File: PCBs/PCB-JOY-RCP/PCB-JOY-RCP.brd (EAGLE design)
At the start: 30 x 25.9 mm, 20 parts, among them IC1 ADS7828

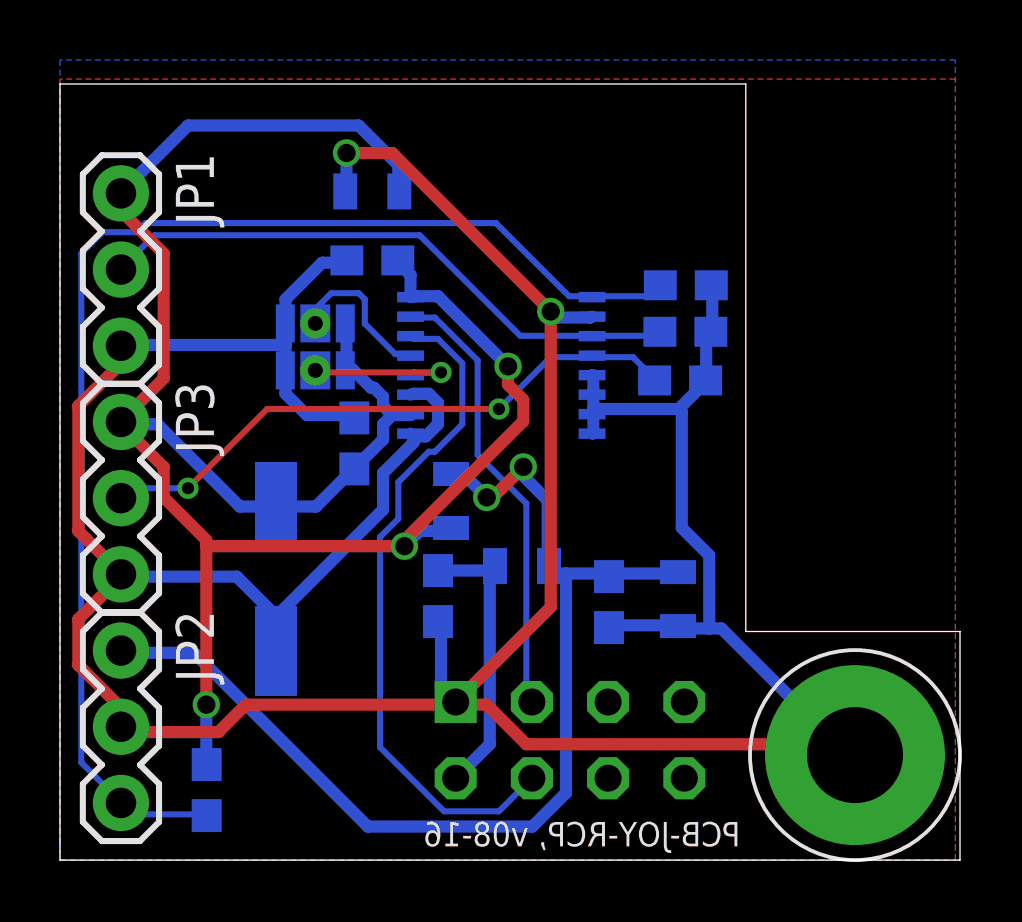
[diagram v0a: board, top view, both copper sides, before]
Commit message: Added SKAARHOJ_ID to a lot of PCBs...
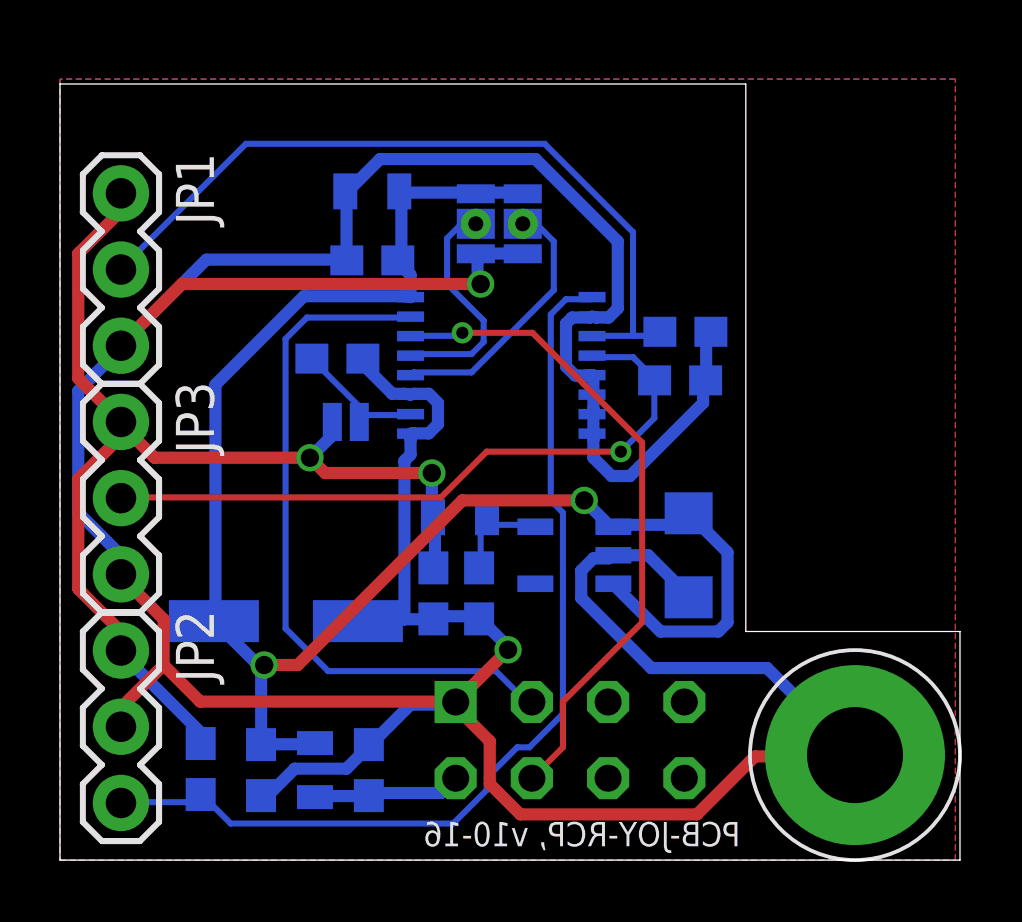
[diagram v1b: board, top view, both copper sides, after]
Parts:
- removed C9: 22uF, SparkFun:0805
- removed PC2: 47u, rcl:PANASONIC_D
- added C23: 10uF 6.3V A TANT, freetronics:EIA3216
- added C5: 100nF, SparkFun:0603-CAP
- added PC1: 330uF, rcl:PANASONIC_D
- added SJ1: SOLDERJUMPERNO, SparkFun:SJ_2S-NO
- added U2: MIC5205-3.3YM5, microbuilder:SOT23-5
- C4: value 10n -> 100nF
- moved C10 12.9 mm to (6.70, 3.00)
- moved C4 12.4 mm to (14.0, 8.89), turned to 270 degrees
- moved L4 9.69 mm to (8.50, 3.00), turned to 90 degrees
- moved U$19 6.30 mm to (13.9, 21.2), turned to 0 degrees
- moved C12 6.24 mm to (10.3, 3.00), turned to 90 degrees
- moved C1 2.88 mm to (9.24, 16.7), turned to 180 degrees
- moved R2 0.73 mm to (4.69, 3.04)
- moved L1 0.62 mm to (13.3, 11.4), turned to 0 degrees
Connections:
- removed net 5V_AD: C1.1, C2.1, C3.1, IC1.10, IC1.16, JP1.1, JP3.1, L1.1, PC2.+, R2.1, U$19.H0, U$19.H1
- new net N$1: C1.1, IC1.10, SJ1.2
- new net N$3: C4.1, L1.1, U2.5
- new net REF: C5.1, JP1.1, JP2.1, JP3.1, L1.2, R2.1, SJ1.1
- net 5V: now also C2.1, C23.A, C3.1, IC1.16, PC1.+, U$19.H0, U$19.H1, U2.1, U2.3; no longer C9.1, JP2.1, L1.2
- net FRONT: no longer C4.1
- net GND: now also C23.C, C5.2, PC1.-, U2.2; no longer C9.2, PC2.-
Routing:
- net 5V_AD: track 71.5 -> 0.00 mm, vias 3 -> 0
- net REF: track 0.00 -> 37.7 mm, vias 0 -> 2
- net 5V: track 36.4 -> 56.0 mm
- net FRONT: track 42.8 -> 32.1 mm
- net GND: track 129.9 -> 139.7 mm
- net I2C_SDA: track 15.0 -> 23.4 mm
- net JOY_1: track 19.9 -> 25.8 mm
- net N$1: track 0.00 -> 4.85 mm
- net ARD_5V: track 9.55 -> 4.93 mm
- net A0: track 5.33 -> 8.91 mm, vias 1 -> 0
- net N$3: track 0.00 -> 3.54 mm
- net A1: track 5.26 -> 7.81 mm
- net JOY_2: track 20.1 -> 22.6 mm, vias 2 -> 1
- net I2C_SCL: track 22.6 -> 22.0 mm, vias 0 -> 1
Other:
- board text added: "PCB-JOY-RCP, v10-16"
- board text removed: "PCB-JOY-RCP, v08-16"

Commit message: PCB updates
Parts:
- added U$1: GNDPAD6MM, SKAARHOJ:3.2MMPAD6MM
- moved U$6 53.7 mm to (3.50, 52.0), turned to 180 degrees
- moved SERIAL 45.1 mm to (13.0, 49.0), turned to 90 degrees
- moved C10 41.2 mm to (13.8, 43.6), turned to 90 degrees
- moved L4 40.8 mm to (12.0, 43.6), turned to 270 degrees
- moved C12 40.6 mm to (10.2, 43.6), turned to 270 degrees
- moved R2 30.5 mm to (16.3, 31.2), turned to 180 degrees
- moved PC1 30.3 mm to (11.7, 38.0), turned to 180 degrees
- moved C23 24.5 mm to (10.4, 32.2), turned to 0 degrees
- moved JP2 22.2 mm to (16.5, 23.8), turned to 90 degrees
- moved JP1 20.0 mm to (16.5, 8.51), turned to 90 degrees
- moved U2 19.5 mm to (10.4, 28.4), turned to 180 degrees
- moved U$19 18.8 mm to (16.1, 2.54), turned to 180 degrees
- moved C4 16.5 mm to (11.7, 25.2), turned to 180 degrees
- moved C6 15.1 mm to (9.15, 8.04), turned to 0 degrees
- moved C5 14.8 mm to (11.7, 23.7), turned to 180 degrees
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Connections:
- net GND: now also U$1.P$1
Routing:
- net I2C_SCL: track 22.0 -> 42.8 mm
- net I2C_SDA: track 23.4 -> 39.4 mm, vias 0 -> 1
- net GND: track 139.7 -> 124.1 mm, vias 2 -> 3
- net A0: track 8.91 -> 17.9 mm, vias 0 -> 1
- net 5V: track 56.0 -> 64.7 mm, vias 2 -> 3
- net A1: track 7.81 -> 15.3 mm, vias 0 -> 1
- net JOY_2: track 22.6 -> 17.1 mm, vias 1 -> 2
- net ARD_5V: track 4.93 -> 9.89 mm
- net JOY_1: track 25.8 -> 30.7 mm, vias 0 -> 1
- net FRONT: track 32.1 -> 29.0 mm, vias 0 -> 2
- net REF: track 37.7 -> 40.5 mm, vias 2 -> 1
- net N$1: track 4.85 -> 7.46 mm
- removed copper zone on layer 1, net GND
- removed copper zone on layer 16, net GND
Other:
- board size 30 x 25.9 mm -> 18 x 55.5 mm
- board text added: "PCB-JOY-RCP, v10-16b"
- board text removed: "PCB-JOY-RCP, v10-16"

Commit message: Added cap for silencing the regulator
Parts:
- added C8: 10uF 6.3V A TANT, freetronics:EIA3216
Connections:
- net GND: now also C8.C
- net REF: now also C8.A
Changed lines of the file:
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@@
 </element>
 <element name="U$1" library="SKAARHOJ" package="3.2MMPAD6MM" value="GNDPAD6MM" x="3.5" y="3.5" rot="R180"/>
+<element name="C8" library="freetronics" package="EIA3216" value="10uF 6.3V A TANT" x="-22.86" y="-29.21"/>
 </elements>
 <signals>
@@
 <via x="9.2456" y="12.9032" extent="1-16" drill="0.6096"/>
 <via x="9.2456" y="15.748" extent="1-16" drill="0.6096"/>
+<contactref element="C8" pad="C"/>
+<wire x1="3.5" y1="3.5" x2="-24.26" y2="-29.21" width="0" layer="19" extent="1-1"/>
 </signal>
 <signal name="A1">
@@
 <wire x1="13.4112" y1="22.7584" x2="13.3096" y2="22.86" width="0.3048" layer="16"/>
 <via x="15.3416" y="6.1976" extent="1-16" drill="0.6096"/>
+<contactref element="C8" pad="A"/>
+<wire x1="15.3416" y1="6.1976" x2="-21.46" y2="-29.21" width="0" layer="19" extent="1-16"/>
 </signal>
 <signal name="N$3">

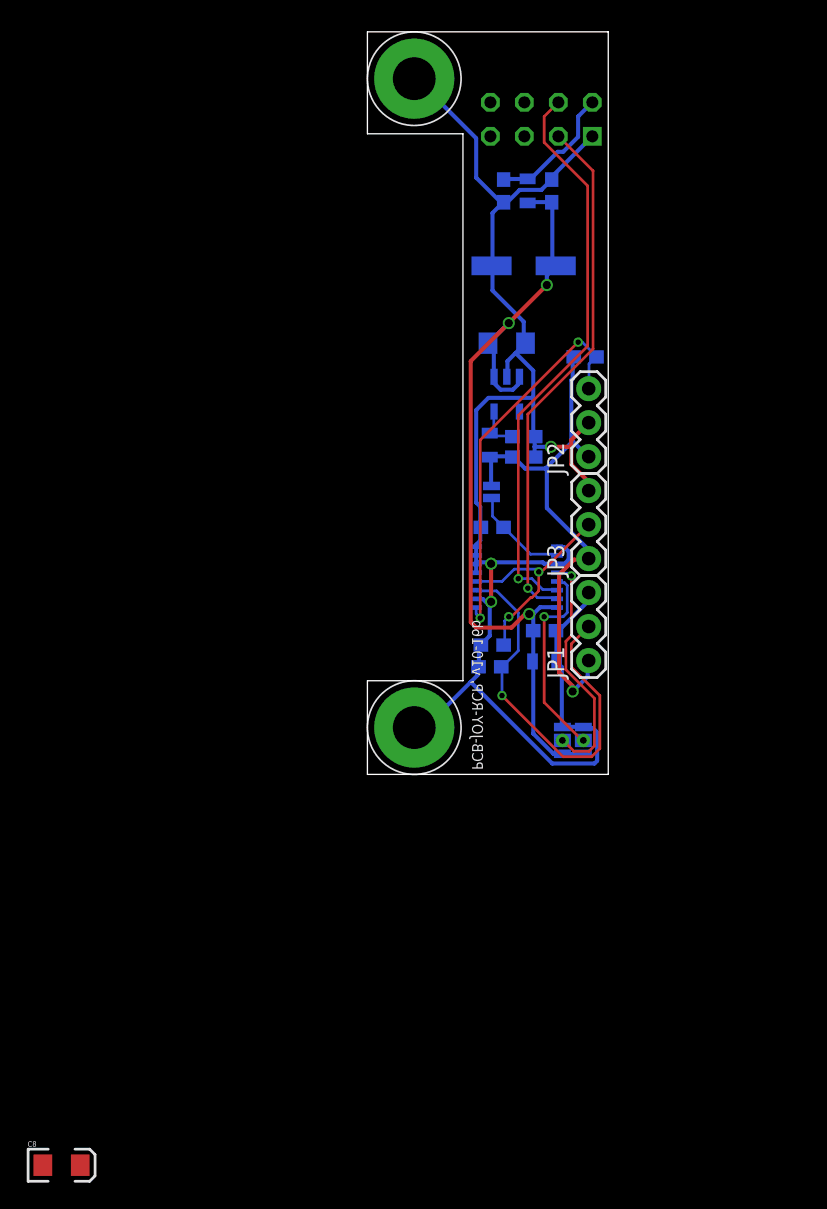
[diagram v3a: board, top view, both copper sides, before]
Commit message: Modified circuitry around AD converter on a number of PCBs
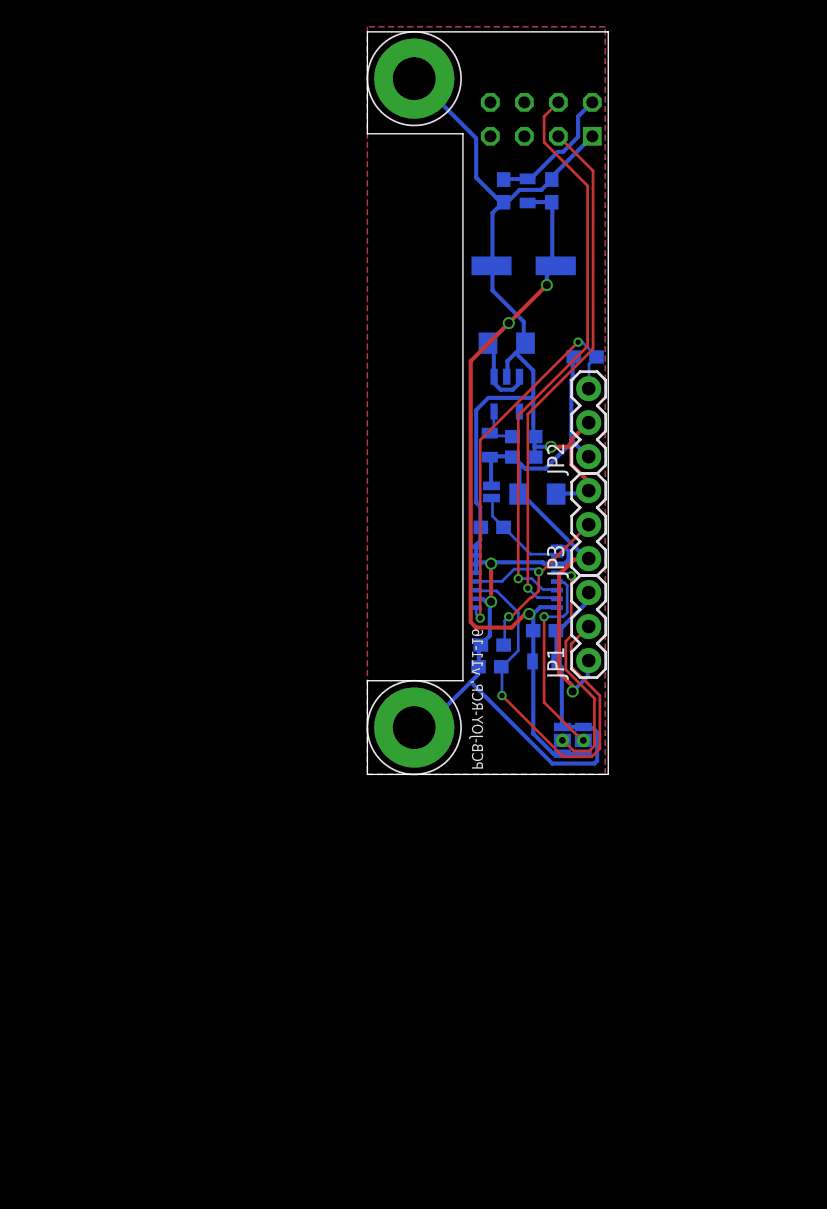
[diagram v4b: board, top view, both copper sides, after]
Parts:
- moved C8 61.5 mm to (12.7, 21.0), flipped to the bottom
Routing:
- net GND: track 124.1 -> 126.7 mm
- net REF: track 40.5 -> 42.8 mm
- added copper zone on layer 1, net GND
- added copper zone on layer 16, net GND
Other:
- board text added: "PCB-JOY-RCP, v11-16"
- board text removed: "PCB-JOY-RCP, v10-16b"
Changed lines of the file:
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@@
 <plain>
 <wire x1="18" y1="55.5" x2="0" y2="55.5" width="0" layer="20"/>
-<text x="7.823" y="0.335" size="0.8128" layer="121" ratio="12" rot="MR90">PCB-JOY-RCP, v10-16b</text>
+<text x="7.823" y="0.335" size="0.8128" layer="121" ratio="12" rot="MR90">PCB-JOY-RCP, v11-16</text>
 <wire x1="0" y1="0" x2="18" y2="0" width="0" layer="20"/>
 <wire x1="18" y1="55.5" x2="18" y2="0" width="0" layer="20"/>
@@
 </element>
 <element name="U$1" library="SKAARHOJ" package="3.2MMPAD6MM" value="GNDPAD6MM" x="3.5" y="3.5" rot="R180"/>
-<element name="C8" library="freetronics" package="EIA3216" value="10uF 6.3V A TANT" x="-22.86" y="-29.21"/>
+<element name="C8" library="freetronics" package="EIA3216" value="10uF 6.3V A TANT" x="12.7" y="20.955" rot="MR0"/>
 </elements>
 <signals>
@@
 <via x="9.2456" y="15.748" extent="1-16" drill="0.6096"/>
 <contactref element="C8" pad="C"/>
-<wire x1="3.5" y1="3.5" x2="-24.26" y2="-29.21" width="0" layer="19" extent="1-1"/>
+<wire x1="16.375" y1="21" x2="14.125" y2="21" width="0.3048" layer="16"/>
+<wire x1="16.5" y1="21.125" x2="16.375" y2="21" width="0.3048" layer="16"/>
+<wire x1="14.125" y1="21" x2="14.1" y2="20.955" width="0.3048" layer="16"/>
+<wire x1="16.5" y1="21.125" x2="16.538" y2="21.21" width="0.3048" layer="16"/>
+<polygon width="0.254" layer="1">
+<vertex x="0" y="0"/>
+<vertex x="17.78" y="0"/>
+<vertex x="17.78" y="55.88"/>
+<vertex x="0" y="55.88"/>
+</polygon>
+<polygon width="0.254" layer="16">
+<vertex x="0" y="0"/>
+<vertex x="17.78" y="0"/>
+<vertex x="17.78" y="55.88"/>
+<vertex x="0" y="55.88"/>
+</polygon>
 </signal>
 <signal name="A1">
@@
 <wire x1="15.3416" y1="31.1912" x2="15.42" y2="31.205" width="0.3048" layer="16"/>
 <wire x1="16.4592" y1="23.7744" x2="16.538" y2="23.75" width="0.3048" layer="16"/>
-<wire x1="11.7856" y1="22.86" x2="10.9728" y2="23.6728" width="0.3048" layer="16"/>
+<wire x1="11.7856" y1="22.86" x2="11.4478" y2="23.1978" width="0.3048" layer="16"/>
+<wire x1="11.4478" y1="23.1978" x2="10.9728" y2="23.6728" width="0.3048" layer="16"/>
 <wire x1="13.3096" y1="22.86" x2="11.7856" y2="22.86" width="0.3048" layer="16"/>
 <wire x1="15.3416" y1="24.892" x2="13.3096" y2="22.86" width="0.3048" layer="16"/>
 <wire x1="10.9728" y1="23.6728" x2="10.835" y2="23.72" width="0.3048" layer="16"/>
 <wire x1="16.4592" y1="16.8656" x2="16.4592" y2="16.1544" width="0.3048" layer="16"/>
-<wire x1="13.4112" y1="19.9136" x2="16.4592" y2="16.8656" width="0.3048" layer="16"/>
-<wire x1="13.4112" y1="22.7584" x2="13.4112" y2="19.9136" width="0.3048" layer="16"/>
 <wire x1="16.4592" y1="16.1544" x2="16.538" y2="16.13" width="0.3048" layer="16"/>
-<wire x1="13.4112" y1="22.7584" x2="13.3096" y2="22.86" width="0.3048" layer="16"/>
 <via x="15.3416" y="6.1976" extent="1-16" drill="0.6096"/>
 <contactref element="C8" pad="A"/>
-<wire x1="15.3416" y1="6.1976" x2="-21.46" y2="-29.21" width="0" layer="19" extent="1-16"/>
+<wire x1="11.375" y1="23.125" x2="11.375" y2="21" width="0.3048" layer="16"/>
+<wire x1="11.375" y1="21" x2="11.3" y2="20.955" width="0.3048" layer="16"/>
+<wire x1="11.375" y1="23.125" x2="11.4478" y2="23.1978" width="0.3048" layer="16"/>
+<wire x1="16.375" y1="16.125" x2="11.5" y2="21" width="0.3048" layer="16"/>
+<wire x1="11.5" y1="21" x2="11.3" y2="20.955" width="0.3048" layer="16"/>
+<wire x1="16.375" y1="16.125" x2="16.538" y2="16.13" width="0.3048" layer="16"/>
 </signal>
 <signal name="N$3">

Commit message: d
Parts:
- removed C23: 10uF 6.3V A TANT, freetronics:EIA3216
- removed C4: 100nF, SparkFun:0603-CAP
- removed L1: ILHB0805ER121V, SparkFun:0805
- added C11: 1nF, SparkFun:0603-CAP
- added C9: 10uF 6.3V A TANT, freetronics:EIA3216
- added U$2: JST-SM03B-GHS-TB, SKAARHOJ:JST-SM03B-GHS-TB
- added U$3: SM06B-SRSS-TB, SKAARHOJ:JST-SM06B-SRSS-TB
- added U$4: GNDPAD6MM, SKAARHOJ:3.2MMPAD6MM
- SJ1: value SOLDERJUMPERNO -> SOLDERJUMPERNC; device SparkFun:SJ_2S-NO -> SparkFun:SJ_2S
- moved U2 0.86 mm to (11.2, 28.2)
- moved SJ1 0.63 mm to (8.63, 21.1)
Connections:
- removed net N$3: C4.1, L1.1, U2.5
- new net N$11: U$3.P6
- new net N$2: C11.1, U2.4
- net 5V: now also C9.A; no longer C23.A
- net FRONT: now also U$3.P4
- net GND: now also C11.2, C9.C, U$2.P1, U$3.P1, U$3.P5, U$4.P$1; no longer C23.C, C4.2
- net JOY_1: now also U$2.P2
- net JOY_2: now also U$3.P2
- net REF: now also U$2.P3, U$3.P3, U2.5; no longer L1.2
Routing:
- net REF: track 42.8 -> 63.4 mm, vias 1 -> 3
- net GND: track 126.7 -> 147.0 mm, vias 3 -> 2
- net FRONT: track 29.0 -> 47.8 mm
- net JOY_2: track 17.1 -> 20.8 mm, vias 2 -> 3
- net N$3: track 3.53 -> 0.00 mm
- net JOY_1: track 30.7 -> 33.1 mm, vias 1 -> 2
- net N$2: track 0.00 -> 1.85 mm
- net A0: track 17.9 -> 16.1 mm, vias 1 -> 3
- net 5V: track 64.7 -> 65.6 mm, vias 3 -> 4
- net I2C_SCL: track 42.8 -> 42.0 mm, vias 1 -> 3
- net I2C_SDA: track 39.4 -> 38.6 mm
- net N$1: track 7.46 -> 8.27 mm
- net A1: track 15.3 -> 15.2 mm, vias 1 -> 3
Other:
- board size 18 x 55.5 mm -> 21.8 x 55.5 mm
- board text added: "PCB-JOY-RCP, v02-17"
- board text added: "RED BLACK WHITE GRAY ORANGE WHITE GRAY ORANGE"
- board text added: "white gray orange"
- board text added: "white gray orange red black (Blank)"
- board text removed: "PCB-JOY-RCP, v11-16"

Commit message: update
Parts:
- moved U$2 29.2 mm to (25.4, 19.7), flipped to the bottom
- moved U$3 21.6 mm to (21.6, 11.4), flipped to the bottom
- moved U$1 14.6 mm to (18.1, 3.50), flipped to the bottom
- moved U$6 14.6 mm to (18.1, 52.0), flipped to the bottom
- moved JP1 11.5 mm to (5.05, 8.51), flipped to the bottom
- moved JP2 11.5 mm to (5.05, 23.8), flipped to the bottom
- moved JP3 11.5 mm to (5.05, 16.1), flipped to the bottom
- moved R2 10.9 mm to (5.32, 31.2), flipped to the top
- moved U$19 10.7 mm to (5.45, 2.54), flipped to the top
- moved C11 6.35 mm to (7.62, 27.9), flipped to the top
- moved C10 5.96 mm to (7.82, 43.6), flipped to the top
- moved C9 5.08 mm to (13.3, 27.9), flipped to the top
- moved C2 4.89 mm to (8.35, 10.7), flipped to the top
- moved C3 4.89 mm to (8.35, 8.45), flipped to the top
- moved SERIAL 4.41 mm to (8.59, 49.0), flipped to the top
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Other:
- outline, holes or cut-outs redrawn
